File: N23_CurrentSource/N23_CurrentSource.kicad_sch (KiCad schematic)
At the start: 62 parts

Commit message: Updates, add N25
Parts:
- added JP1: A, symbol Jumper:Jumper_2_Small_Open
- added JP2: B, symbol Jumper:Jumper_2_Small_Open
- K1: footprint Philips_PM2528:PM2528_RiserCardConnector -> PM2528:PM2528_RiserCardConnector
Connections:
- net at A2301.2 (-), C2303.2, R2303.2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: now also JP2.2 (B)
- net at R2301.2, R2302.1: now also JP1.1 (A)
- net at R2302.2, R2303.1: now also JP1.2 (B), JP2.1 (A)
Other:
- note added: "Measuring zero"
- note added: "Power"
- note added: "Relais"
- note added: "Supply zero"
- note removed: "A"
- note removed: "B"
- title: N23 Current Source -> Philips PM2528 - N23 (Current Source)
- moved on the sheet: A2301, C2301, C2302, C2303, C2304, C2305, K2301A, K2301B, K2302A, K2302B, K2303A, K2303B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

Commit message: Update schematics, move projectlibraries to D:
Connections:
- net GND4: now also K2301.6, K2302.6, K2303.6, K2304.6, K2305.6, K2306.6, K2307.6; no longer K2301.2, K2302.2, K2303.2, K2304.2, K2305.2, K2306.2, K2307.2
- net REL2301: now also K2301.10; no longer K2301.1
- net REL2302: now also K2302.10; no longer K2302.1
- net REL2303: now also K2303.10; no longer K2303.1
- net REL2304: now also K2304.10; no longer K2304.1
- net REL2305: now also K2305.10; no longer K2305.1
- net REL2306: now also K2306.10; no longer K2306.1
- net REL2307: now also K2307.10; no longer K2307.1
- net at R2313.2: now also K2303.1; no longer K2303.4
- net at K2306.5, R2326.1, R2328.1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: now also K2307.1; no longer K2307.4
- net at C2305.1, R2324.1, V2309.1 (C)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: now also K2305.1; no longer K2305.4
- net at K2301.5, K2302.5, K2303.5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: now also K2306.1; no longer K2306.4
- net at R2309.2: now also K2304.1; no longer K2304.4
- net at R2321.2, TP2301.1: now also K2301.1; no longer K2301.4
- net at R2317.2: now also K2302.1; no longer K2302.4
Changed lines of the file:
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@@
 	(title_block
 		(title "Philips PM2528 - N23 (Current Source)")
-		(date "2025-04-05")
+		(date "2025-07-06")
+		(rev "1.0")
 	)
 	(rectangle
@@
 		(pin "5"
 		)
-		(pin "4"
+		(pin "10"
 		)
-		(pin "2"
+		(pin "6"
 		)
 		(instances
@@
 		(pin "5"
 		)
-		(pin "4"
+		(pin "6"
 		)
-		(pin "2"
+		(pin "10"
 		)
 		(instances
@@
 			)
 		)
-		(pin "4"
+		(pin "10"
 		)
 		(pin "1"
 		)
-		(pin "2"
+		(pin "6"
 		)
 		(pin "5"
@@
 		(pin "5"
 		)
-		(pin "4"
+		(pin "6"
 		)
-		(pin "2"
+		(pin "10"
 		)
 		(instances
@@
 		(pin "5"
 		)
-		(pin "4"
+		(pin "10"
 		)
-		(pin "2"
+		(pin "6"
 		)
 		(instances
@@
 			)
 		)
-		(pin "4"
+		(pin "6"
 		)
 		(pin "1"
 		)
-		(pin "2"
+		(pin "10"
 		)
 		(pin "5"
@@
 		(pin "5"
 		)
-		(pin "4"
+		(pin "10"
 		)
-		(pin "2"
+		(pin "6"
 		)
 		(instances
@@
 		(pin "5"
 		)
-		(pin "4"
+		(pin "10"
 		)
-		(pin "2"
+		(pin "6"
 		)
 		(instances
@@
 			)
 		)
-		(pin "4"
+		(pin "10"
 		)
 		(pin "1"
 		)
-		(pin "2"
+		(pin "6"
 		)
 		(pin "5"
@@
 		(pin "5"
 		)
-		(pin "4"
+		(pin "6"
 		)
-		(pin "2"
+		(pin "10"
 		)
 		(instances
@@
 			)
 		)
-		(pin "4"
+		(pin "6"
 		)
 		(pin "1"
 		)
-		(pin "2"
+		(pin "10"
 		)
 		(pin "5"
@@
 			)
 		)
-		(pin "4"
+		(pin "10"
 		)
 		(pin "1"
 		)
-		(pin "2"
+		(pin "6"
 		)
 		(pin "5"
@@
 			)
 		)
-		(pin "4"
+		(pin "10"
 		)
 		(pin "1"
 		)
-		(pin "2"
+		(pin "6"
 		)
 		(pin "5"
@@
 			)
 		)
-		(pin "4"
+		(pin "10"
 		)
 		(pin "1"
 		)
-		(pin "2"
+		(pin "6"
 		)
 		(pin "5"

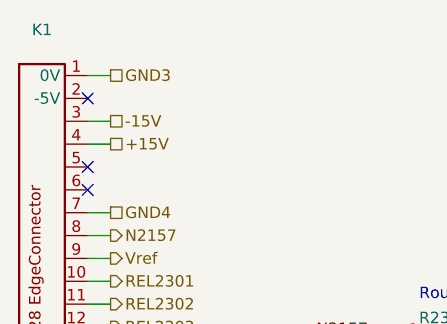
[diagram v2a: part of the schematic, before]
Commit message: Restructure folders, added EPROM-dumps
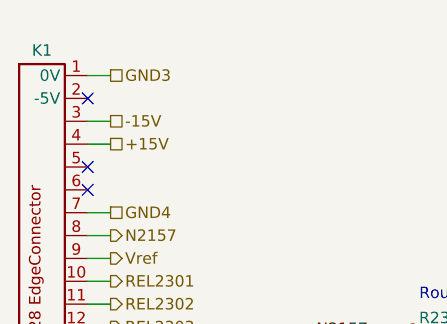
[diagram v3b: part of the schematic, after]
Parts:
- A2301: footprint Package_SO:SOIC-8_3.9x4.9mm_P1.27mm -> Package_TO_SOT_THT:TO-99-8
- C2301, C2302, C2303, C2304, C2305: footprint (none) -> Capacitor_THT:C_Rect_L26.5mm_W8.5mm_P22.50mm_MKS4
- JP1, JP2: footprint (none) -> TestPoint:TestPoint_Bridge_Pitch5.08mm_Drill0.7mm
- K2301, K2302, K2303, K2304, K2305, K2306, K2307: footprint (none) -> PM2528:Reed relay assy
- R2301, R2302, R2303, R2305, R2306, R2307, R2308, R2310, R2311, R2312, R2314, R2315, R2316, R2318, R2319, R2320, R2322, R2323, R2324, R2325, R2326, R2327, R2329, R2330, R2332, R2333: footprint (none) -> Resistor_THT:R_Axial_DIN0207_L6.3mm_D2.5mm_P10.16mm_Horizontal
- R2304, R2309, R2313, R2317, R2321, R2328, R2331: footprint (none) -> PM2528:Potentiometer horizontal ceramic
- TP2301, TP2302, TP2303, TP2304, TP2307, TP2308: footprint (none) -> Connector_PinHeader_1.00mm:PinHeader_1x01_P1.00mm_Vertical
- V2301, V2309: footprint (none) -> Package_TO_SOT_THT:TO-92
